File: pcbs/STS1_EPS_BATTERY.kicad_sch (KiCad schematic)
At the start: 9 parts, among them J6 Battery Pack, U4 BQ29209DRBT

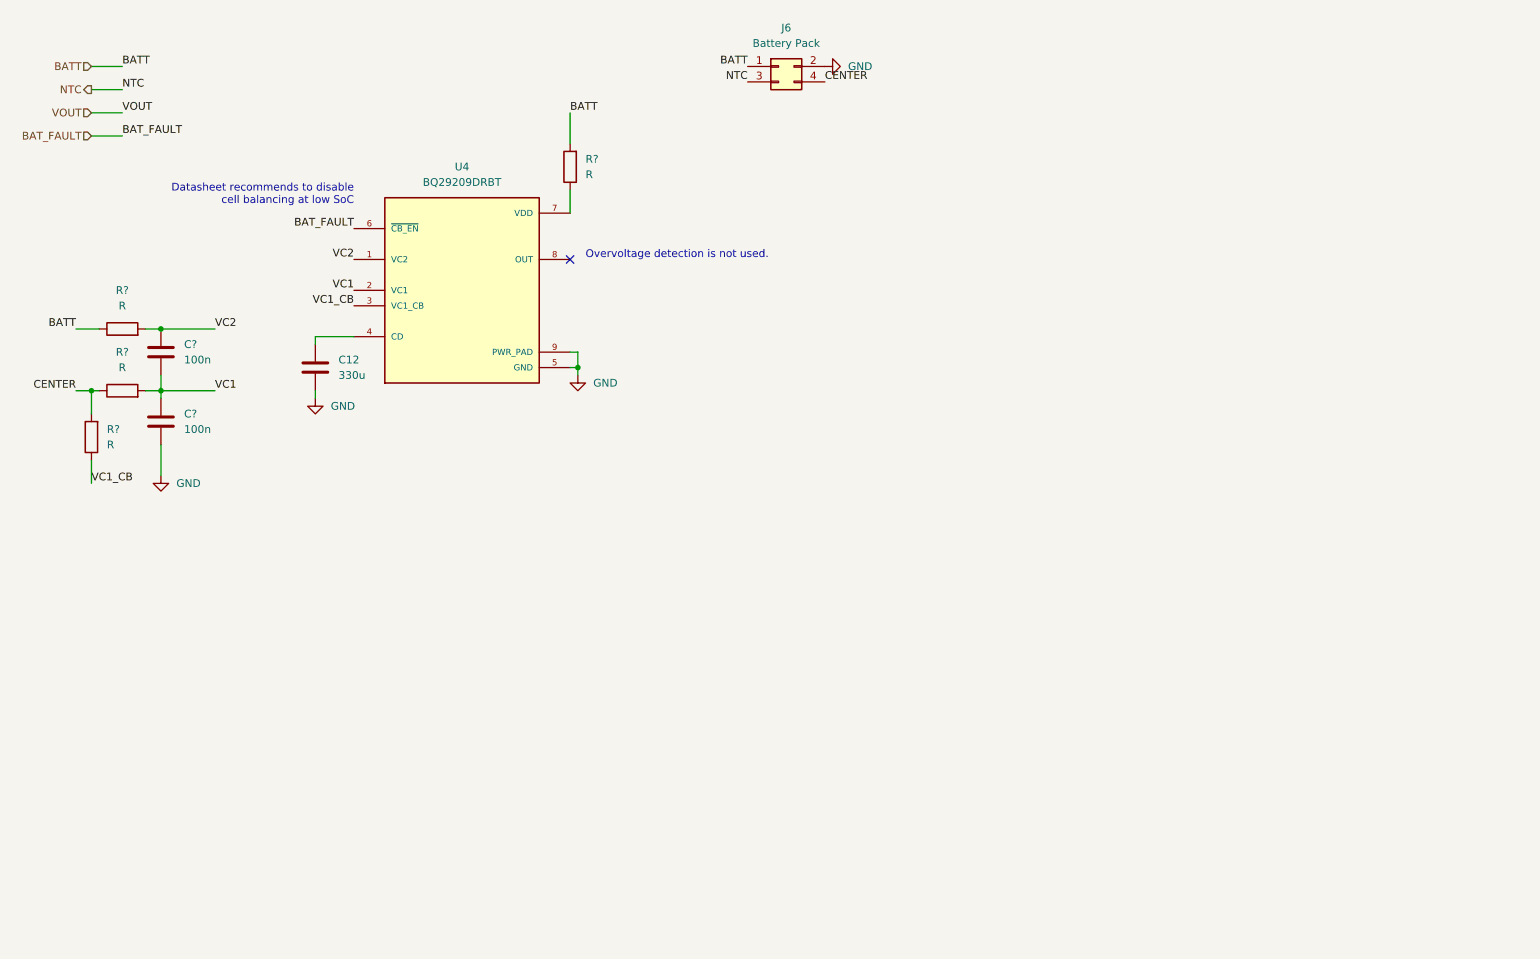
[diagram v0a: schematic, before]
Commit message: Worked on STS1_EPS_1.
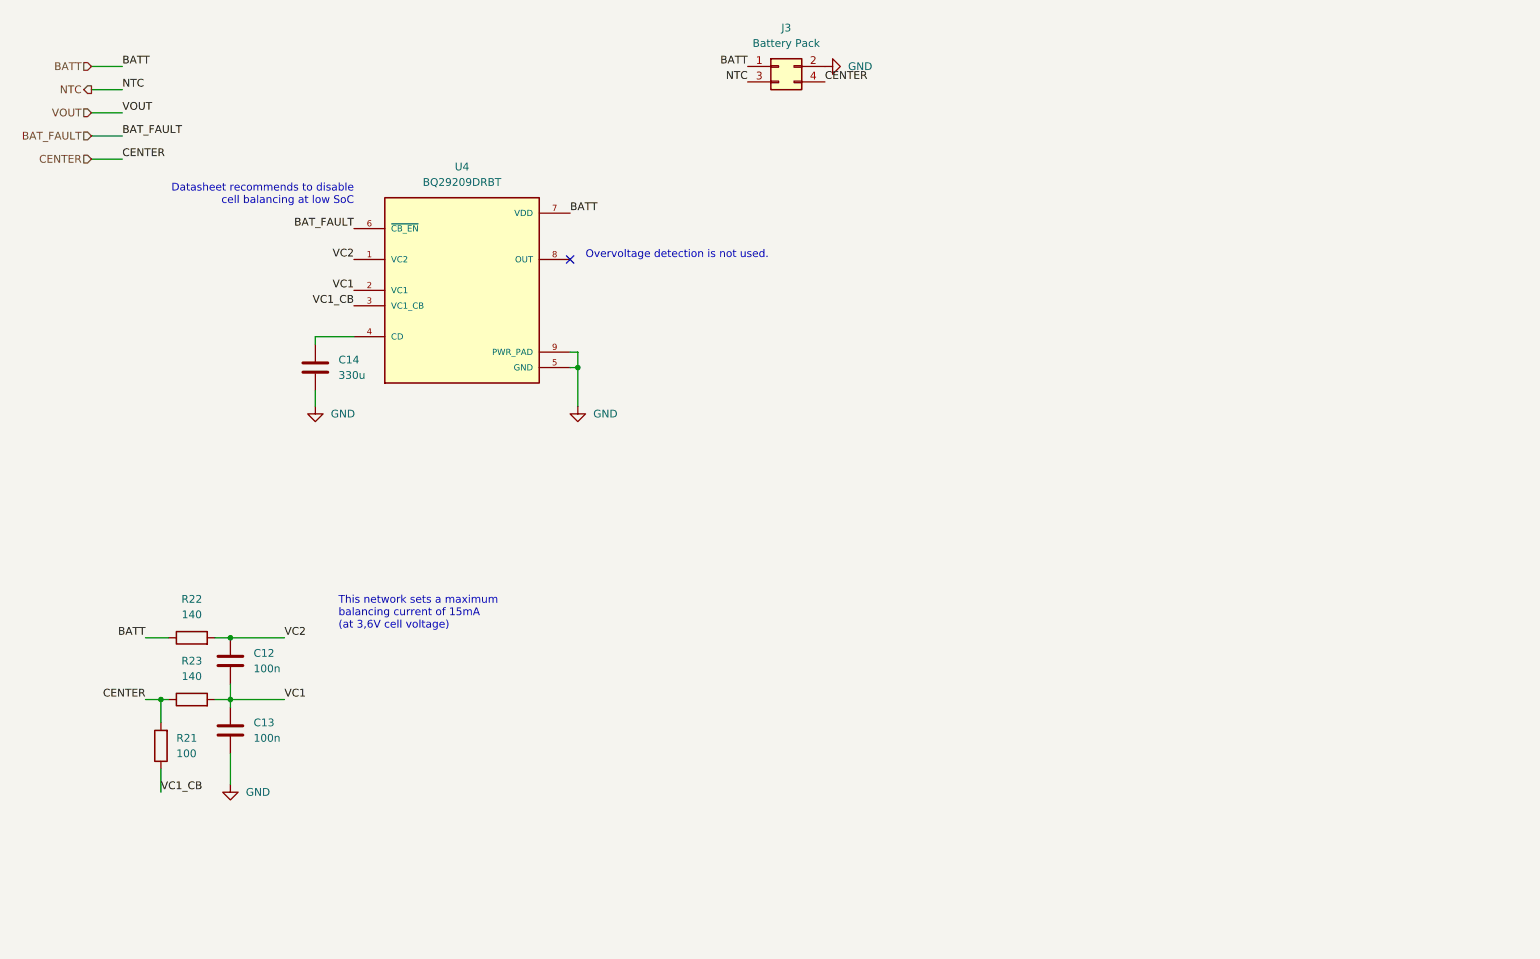
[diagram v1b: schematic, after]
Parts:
- removed R?: R, symbol Device:R
- C12, C13: renamed from C?; footprint (none) -> Capacitor_SMD:C_0805_2012Metric
- J3: renamed from J6; footprint (none) -> STS_Connector:436500415
- R21: renamed from R?; value R -> 100; footprint (none) -> Resistor_SMD:R_0805_2012Metric
- R22, R23: renamed from R?; value R -> 140; footprint (none) -> Resistor_SMD:R_0805_2012Metric
- renumbered C12 to C14
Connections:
- net BATT: now also U4.7 (VDD)
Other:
- note added: "This network sets a maximum balancing current of 15mA (at 3,6V cell voltage)"
- moved on the sheet: C12, C13, R21, R22, R23

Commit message: Worked on STS_EPS_1.
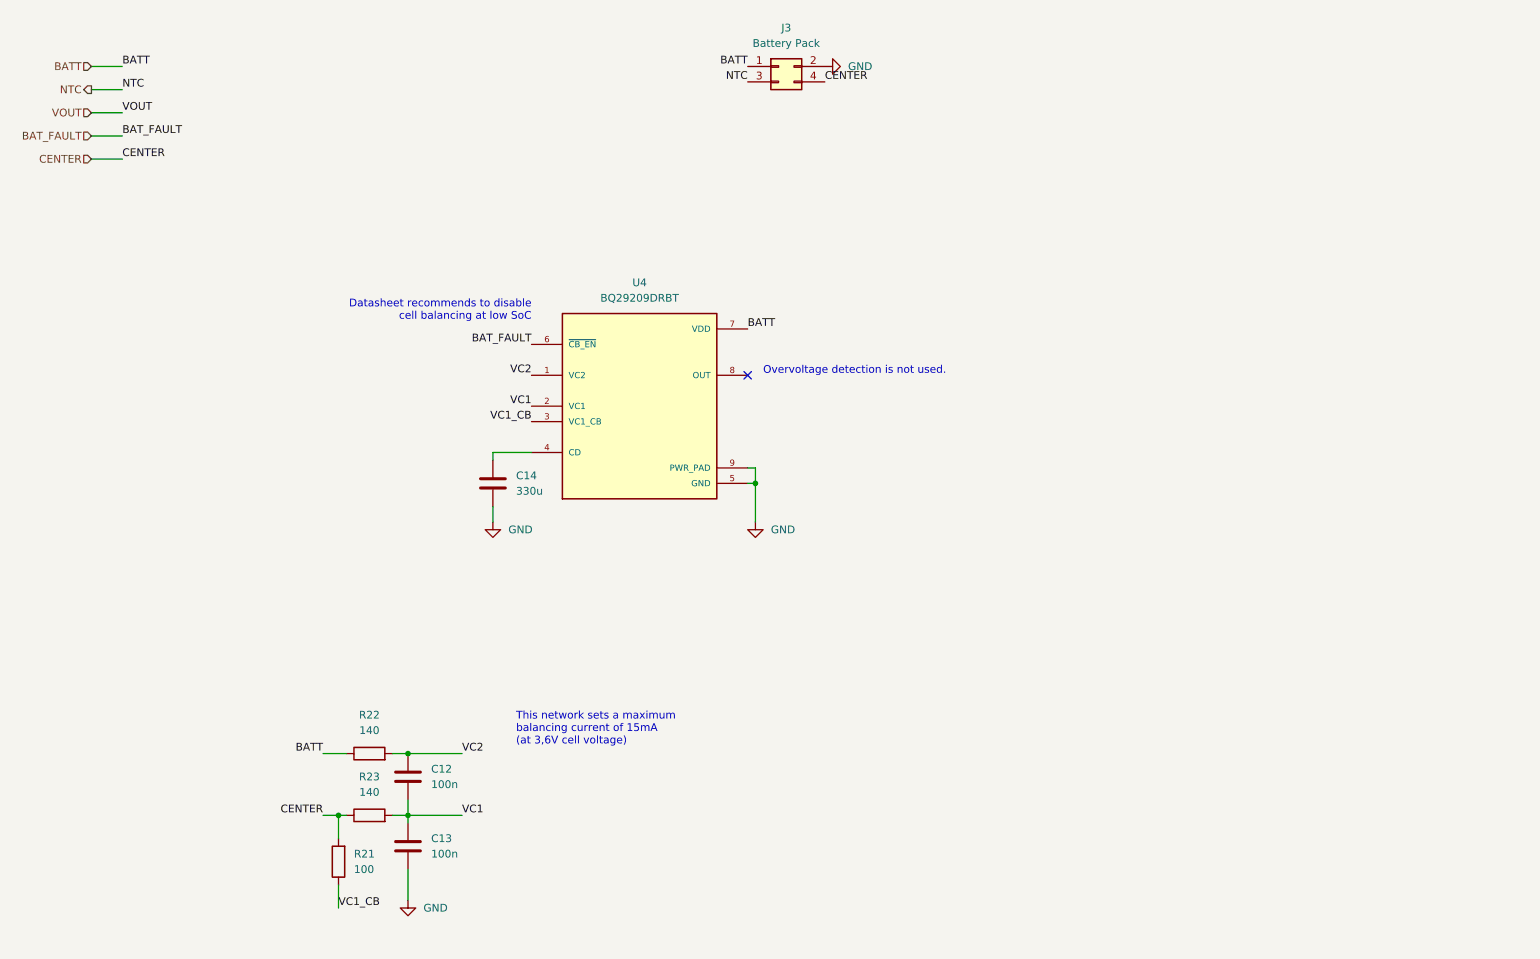
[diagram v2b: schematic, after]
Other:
- moved on the sheet: C12, C13, C14, R21, R22, R23, U4

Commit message: Worked on STS1_EPS_1.
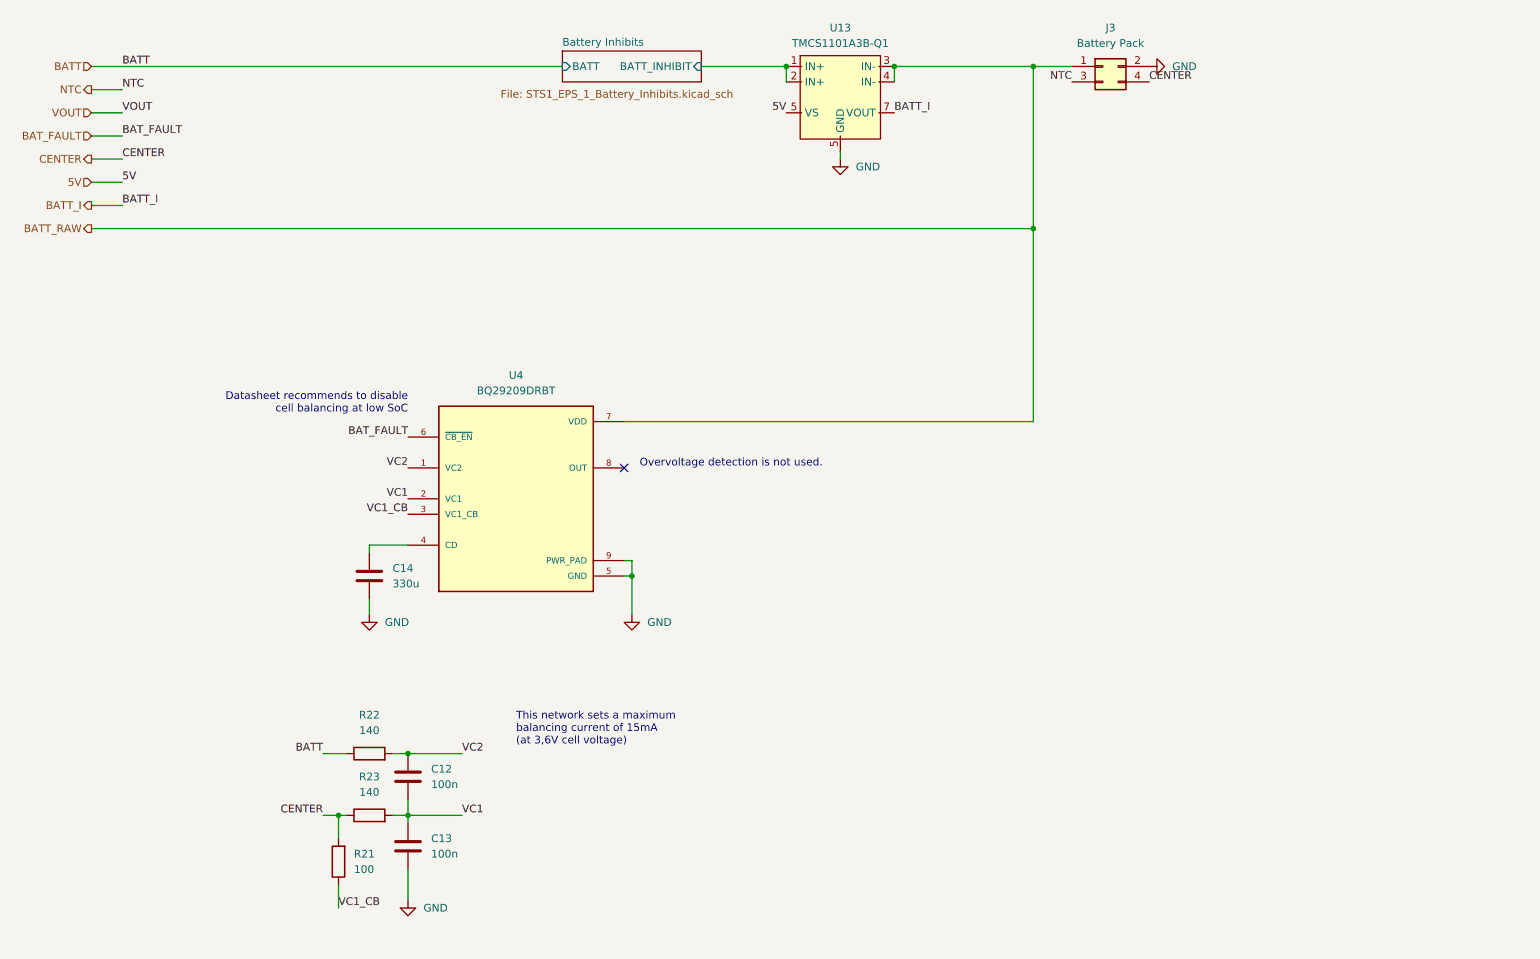
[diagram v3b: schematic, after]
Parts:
- added U13: TMCS1101A3B-Q1, Package_SO:SOIC-8_3.9x4.9mm_P1.27mm, symbol STS_Sensor_Current:TMCS1101Q1
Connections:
- net BATT: no longer J3.1 (Pin_1), U4.7 (VDD)
- net GND: now also U13.5 (VS), U13.6 (NC)
- new net 5V: U13.5 (VS)
- new net BATT_I: U13.7 (VOUT)
- new net BATT_RAW: J3.1 (Pin_1), U13.3 (IN-), U13.4 (IN-), U4.7 (VDD)
- new net Battery Inhibits/BATT_INHIBIT: U13.1 (IN+), U13.2 (IN+)
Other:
- added sheet Battery Inhibits (STS1_EPS_1_Battery_Inhibits.kicad_sch)
- moved on the sheet: C14, J3, U4

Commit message: Worked on STS_EPS_1.
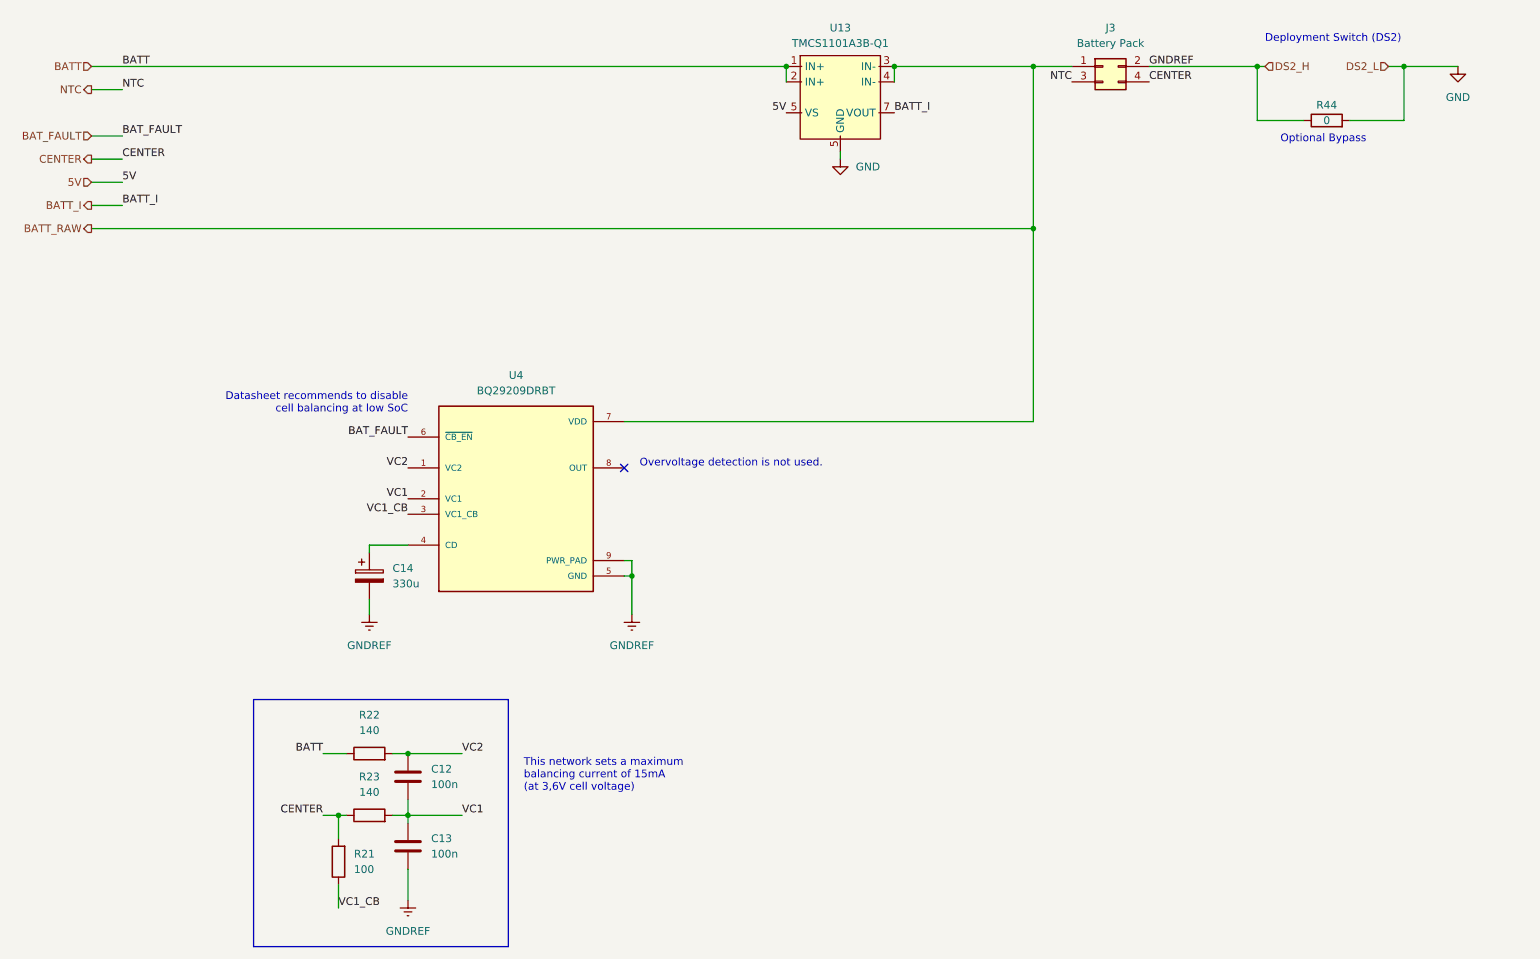
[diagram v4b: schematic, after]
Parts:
- added R44: 0, Resistor_SMD:R_0805_2012Metric, symbol Device:R
- C14: footprint (none) -> Capacitor_Tantalum_SMD:CP_EIA-7343-43_Kemet-X; symbol Device:C -> Device:C_Polarized
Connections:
- net Battery Inhibits/BATT_INHIBIT is gone; now on net BATT: U13.1 (IN+), U13.2 (IN+)
- net GND: now also R44.2; no longer C13.2, C14.2, J3.2 (Pin_2), U4.5 (GND), U4.9 (PWR_PAD)
- new net GNDREF: C13.2, C14.2, J3.2 (Pin_2), R44.1, U4.5 (GND), U4.9 (PWR_PAD)
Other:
- removed sheet Battery Inhibits
- note added: "Deployment Switch (DS2)"
- note added: "Optional Bypass"
